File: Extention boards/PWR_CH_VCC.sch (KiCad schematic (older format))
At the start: 78 parts, among them U1 INA4180, U10 TPS22810, U11 INA4180, U12 LM339, U4 TPS22810, U5 TPS22810, U6 TPS22810, U7 LM339, U8 TPS22810, U9 TPS22810

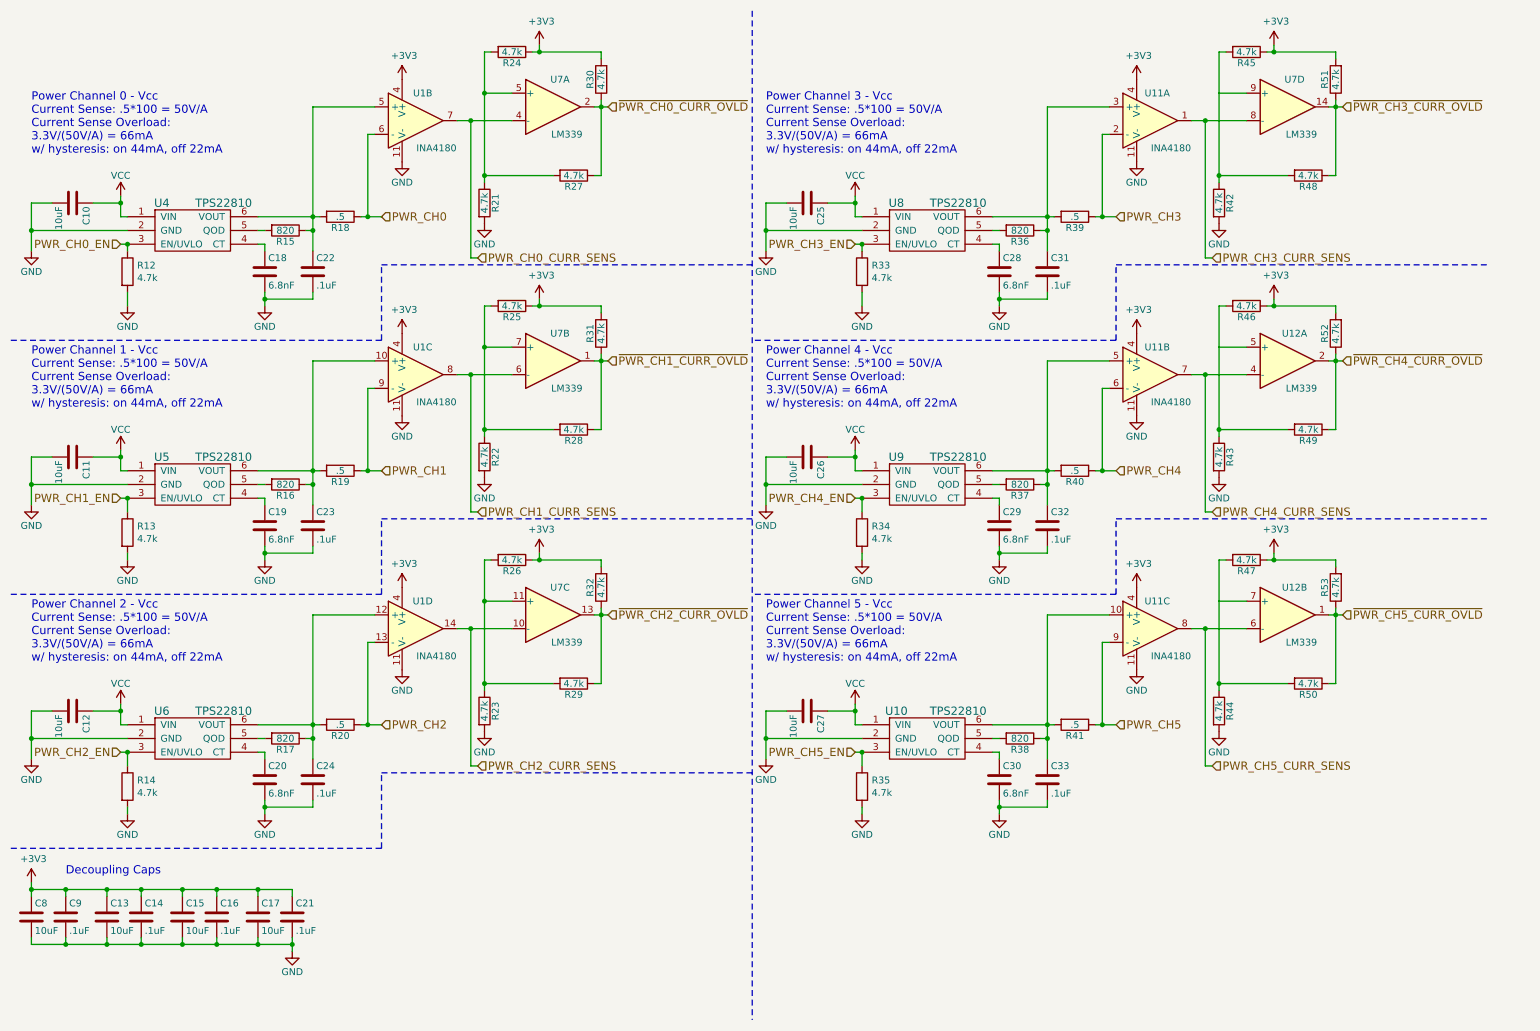
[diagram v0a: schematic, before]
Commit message: New voltage reg, better voltage protection, and consolidated component counts
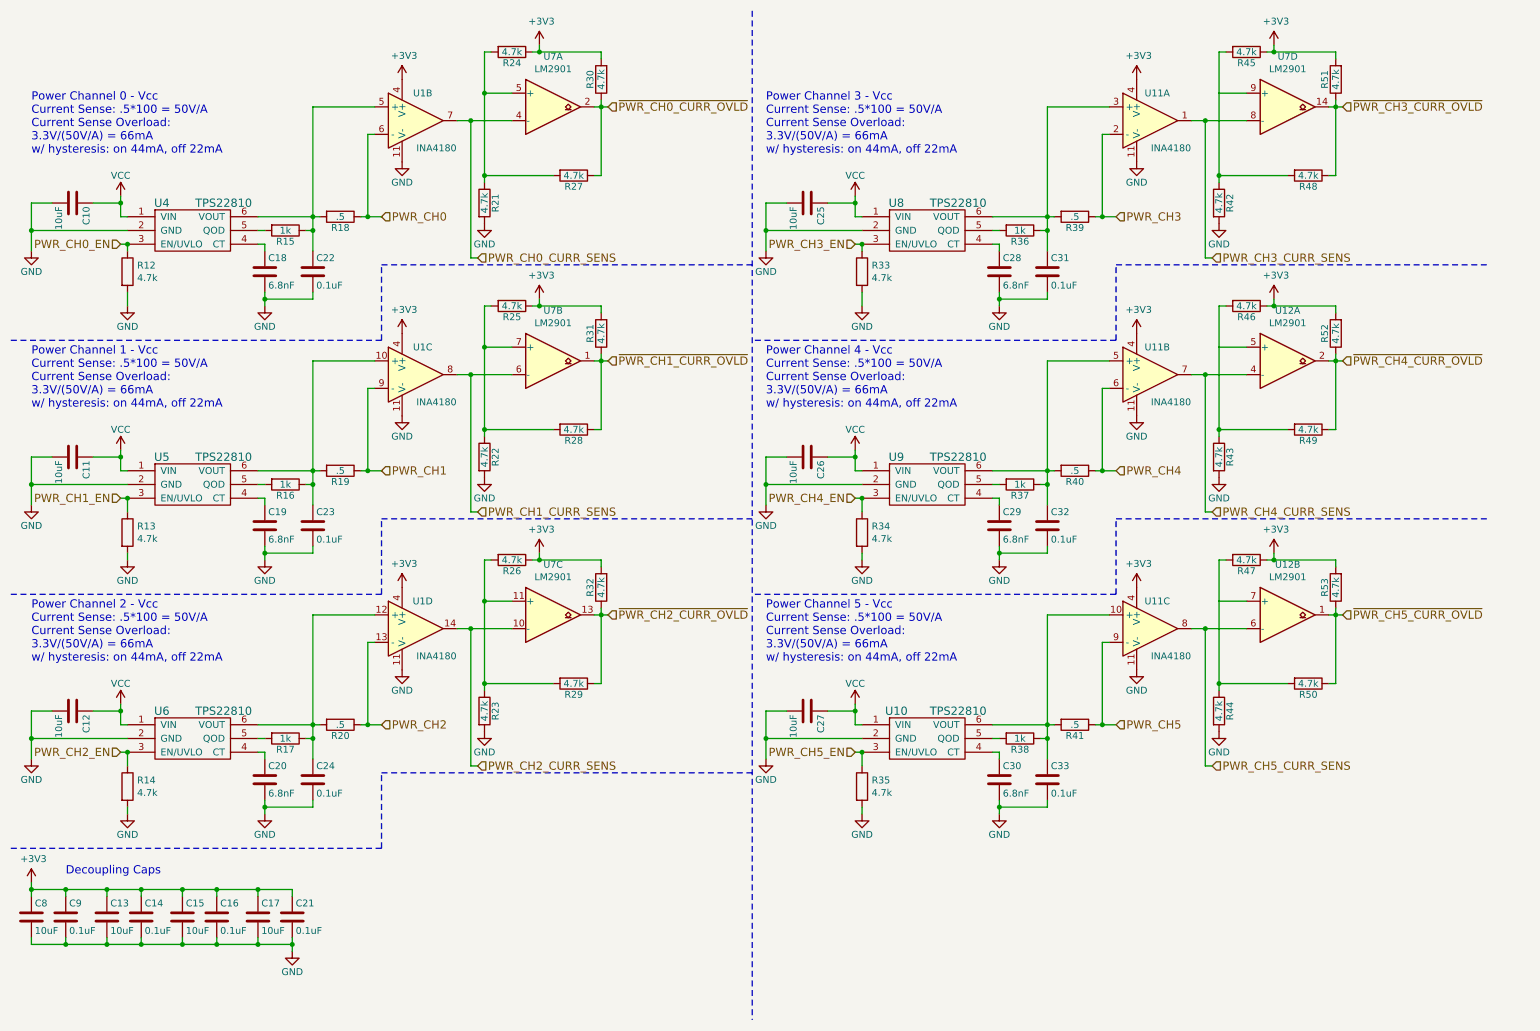
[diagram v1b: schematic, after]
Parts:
- removed U12, U7: LM339, Package_SO:SOIC-14_3.9x8.7mm_P1.27mm, symbol Comparator:LM339
- added U12, U7: LM2901, Package_SO:TSSOP-14_4.4x5mm_P0.65mm, symbol Comparator:LM2901
- C14, C16, C21, C22, C23, C24, C31, C32, C33, C9: value .1uF -> 0.1uF
- R15, R16, R17, R36, R37, R38: value 820 -> 1k
- U1, U11: DigiKey Part Number (none) -> 296-49096-1-ND
- U10, U4, U5, U6, U8, U9: DigiKey Part Number (none) -> 296-45297-1-ND
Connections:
- net PWR_CH0_CURR_SENS: now also U7.4 (-)
- net PWR_CH1_CURR_SENS: now also U7.6 (-)
- net PWR_CH2_CURR_SENS: now also U7.10 (-)
- net PWR_CH3_CURR_SENS: now also U7.8 (-)
- net PWR_CH4_CURR_SENS: now also U12.4 (-)
- net PWR_CH5_CURR_SENS: now also U12.6 (-)
- net ~PWR_CH0_CURR_OVLD: now also U7.2
- net ~PWR_CH1_CURR_OVLD: now also U7.1
- net ~PWR_CH2_CURR_OVLD: now also U7.13
- net ~PWR_CH3_CURR_OVLD: now also U7.14
- net ~PWR_CH4_CURR_OVLD: now also U12.2
- net ~PWR_CH5_CURR_OVLD: now also U12.1
- net at R21.1, R24.2, R27.2: now also U7.5 (+)
- net at R22.1, R25.2, R28.2: now also U7.7 (+)
- net at R23.1, R26.2, R29.2: now also U7.11 (+)
- net at R42.1, R45.2, R48.2: now also U7.9 (+)
- net at R43.1, R46.2, R49.2: now also U12.5 (+)
- net at R44.1, R47.2, R50.2: now also U12.7 (+)
